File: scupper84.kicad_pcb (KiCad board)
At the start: 2 copper layers, 172 parts, among them K1 PG1350, K10 PG1350, K11 PG1350, K12 PG1350, K13 PG1350, K14 PG1350, K15 PG1350, K16 PG1350, K17 PG1350, K18 PG1350, K19 PG1350, K2 PG1350, K20 PG1350, K21 PG1350, K22 PG1350, K23 PG1350, K24 PG1350, K25 PG1350, K26 PG1350, K27 PG1350, K28 PG1350, K29 PG1350, K3 PG1350, K30 PG1350, K31 PG1350, K32 PG1350, K33 PG1350, K34 PG1350, K35 PG1350, K36 PG1350, K37 PG1350, K38 PG1350, K39 PG1350, K4 PG1350, K40 PG1350, K41 PG1350, K42 PG1350, K43 PG1350, K44 PG1350, K45 PG1350, K46 PG1350, K47 PG1350, K48 PG1350, K49 PG1350, K5 PG1350, K50 PG1350, K51 PG1350, K52 PG1350, K53 PG1350, K54 PG1350, K55 PG1350, K56 PG1350, K57 PG1350, K58 PG1350, K59 PG1350, K6 PG1350, K60 PG1350, K61 PG1350, K62 PG1350, K63 PG1350, K64 PG1350, K65 PG1350, K66 PG1350, K67 PG1350, K68 PG1350, K69 PG1350, K7 PG1350, K70 PG1350, K71 PG1350, K72 PG1350, K73 PG1350, K74 PG1350, K75 PG1350, K76 PG1350, K77 PG1350, K78 PG1350, K79 PG1350, K8 PG1350, K80 PG1350, K81 PG1350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

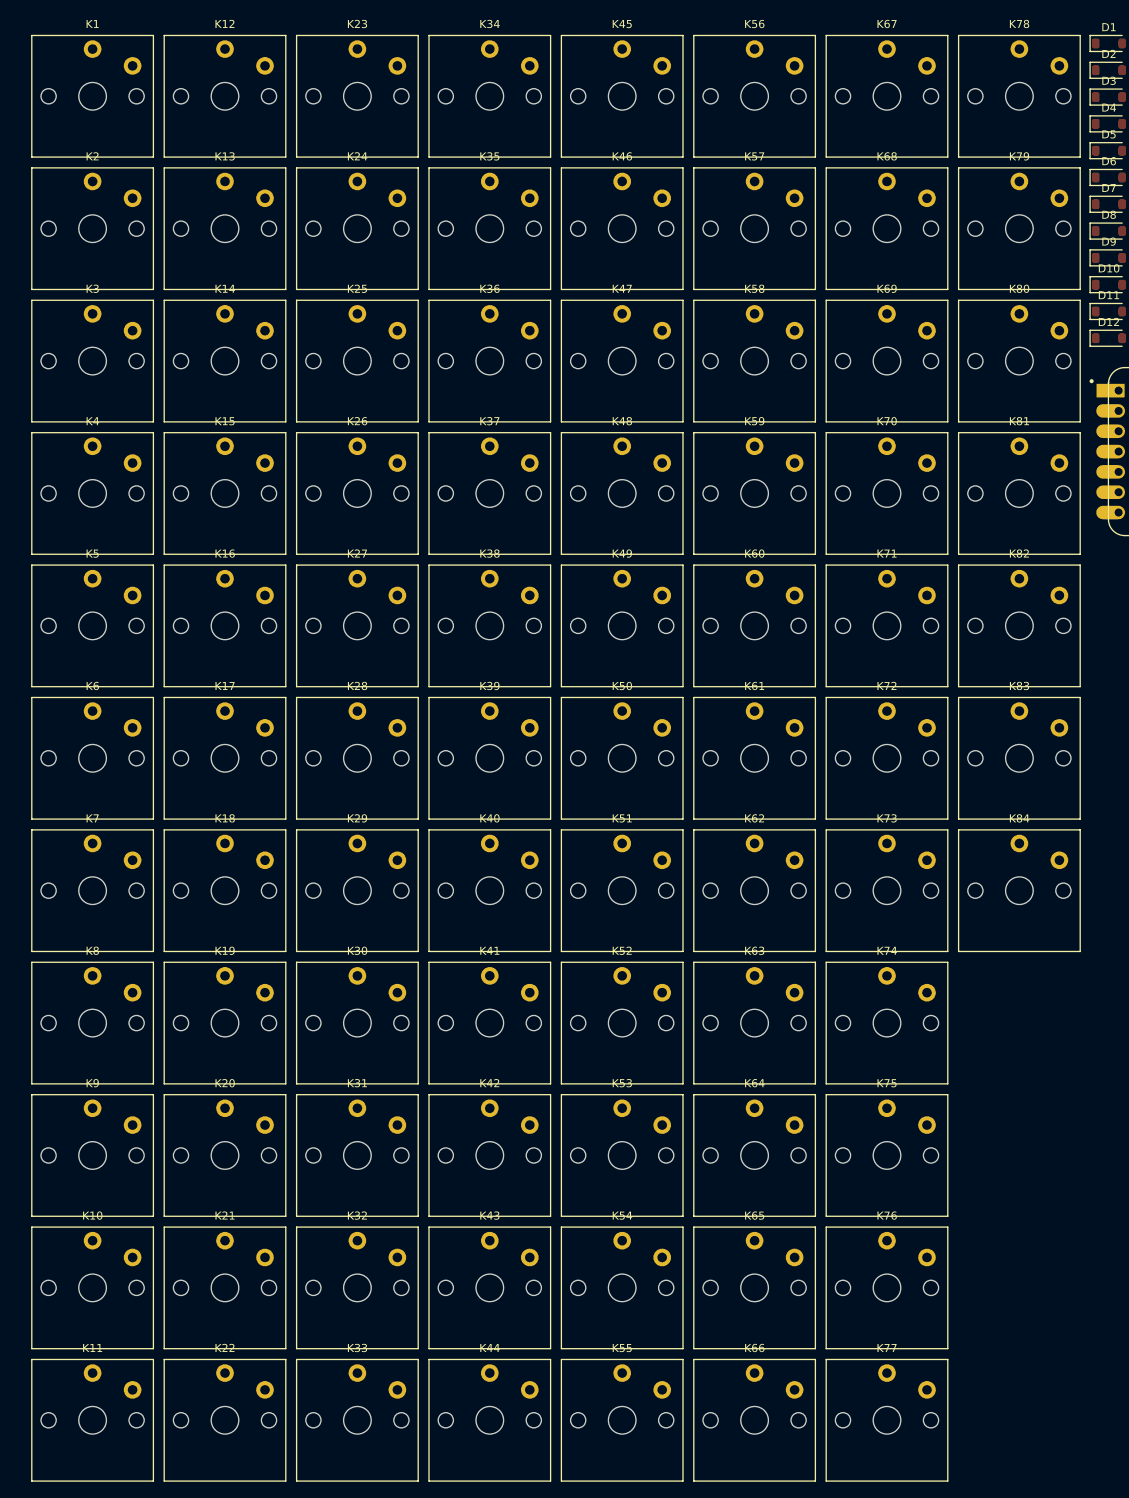
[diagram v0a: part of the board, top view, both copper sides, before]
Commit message: Work in progress on Kailh footprints.
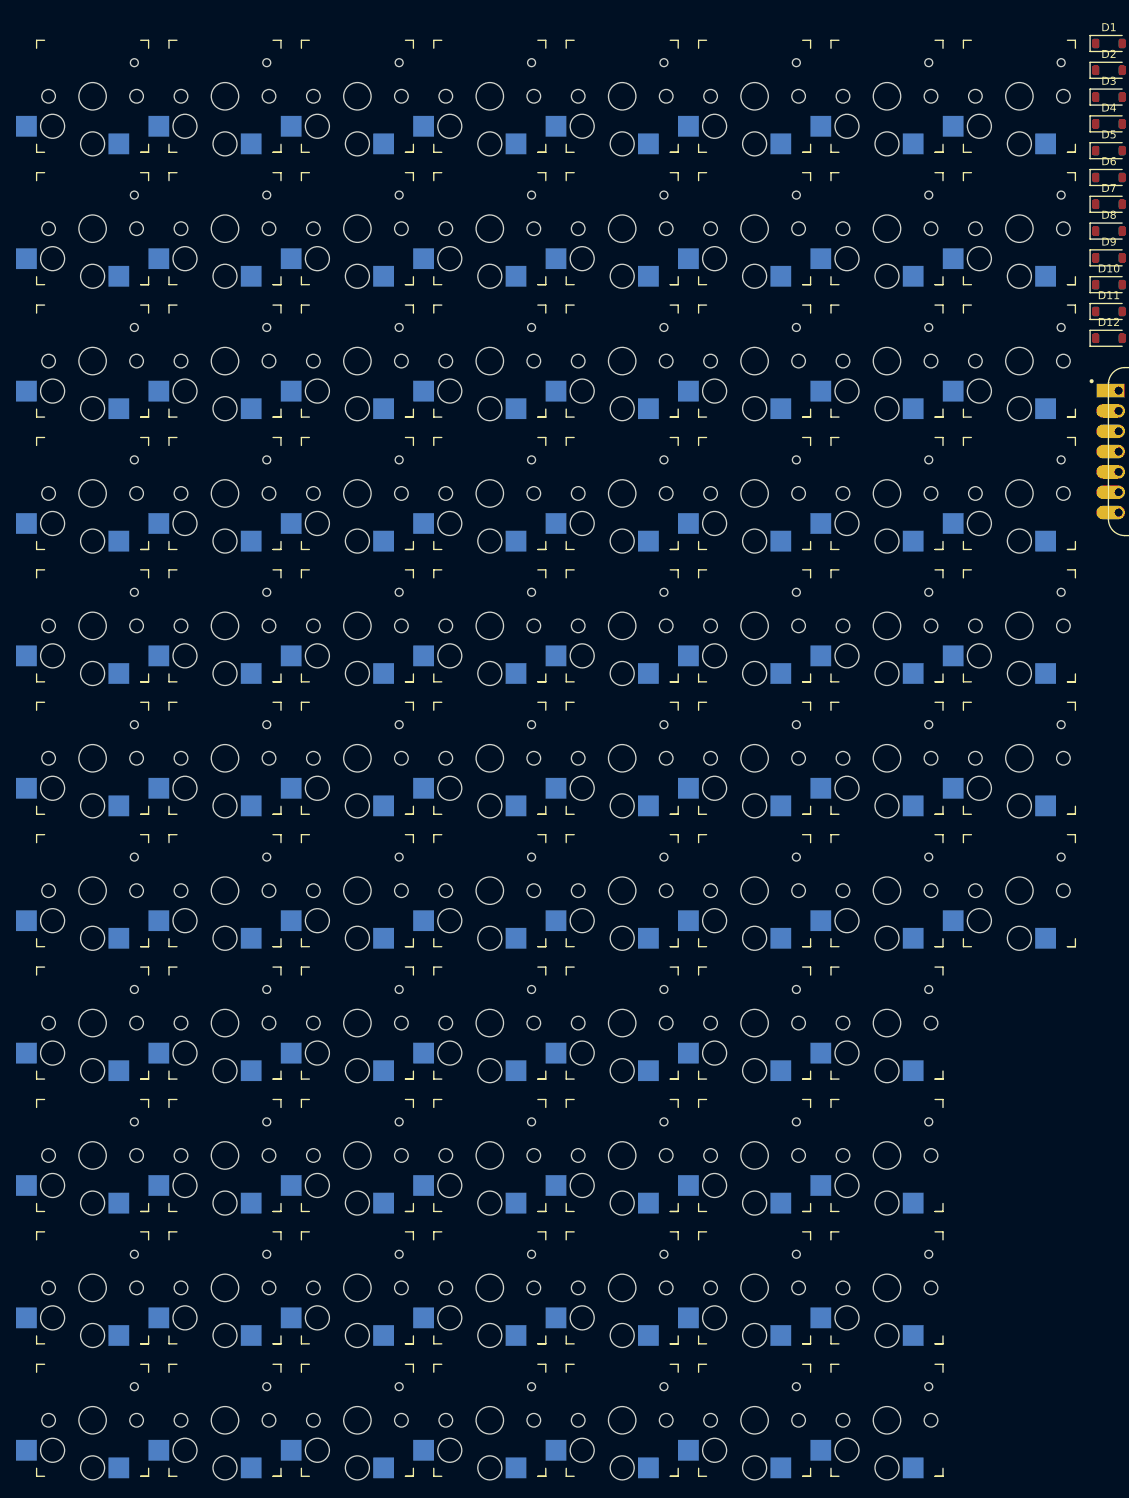
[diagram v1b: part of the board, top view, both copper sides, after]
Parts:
- K1, K10, K11, K12, K13, K14, K15, K16, K17, K18, K19, K2, K20, K21, K22, K23, K24, K25, K26, K27, K28, K29, K3, K30, K31, K32, K33, K34, K35, K36, K37, K38, K39, K4, K40, K41, K42, K43, K44, K45, K46, K47, K48, K49, K5, K50, K51, K52, K53, K54, K55, K56, K57, K58, K59, K6, K60, K61, K62, K63, K64, K65, K66, K67, K68, K69, K7, K70, K71, K72, K73, K74, K75, K76, K77, K78, K79, K8, K80, K81, K82, K83, K84, K9: footprint Switch_Keyboard_Kailh:SW_Kailh_Choc_V1 -> keyswitches:Kailh_socket_PG1350

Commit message: Arranging keys in their staggered array. Keys bigger than 1u may still need some adjustment.
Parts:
- added C1: C, Capacitor_SMD:C_1206_3216Metric_Pad1.33x1.80mm_HandSolder, F.Cu at (134.4, 196.0)
- added D85: 1N4001, Diode_THT:D_DO-41_SOD81_P10.16mm_Horizontal, F.Cu at (119.3, 196.4)
- added DS1: SK6812-E, keyboard_parts:LED_RGB_SK6812Mini-E, F.Cu at (121.6, 143.6)
- added DS10: SK6812-E, keyboard_parts:LED_RGB_SK6812Mini-E, F.Cu at (121.6, 183.2)
- added DS11: SK6812-E, keyboard_parts:LED_RGB_SK6812Mini-E, F.Cu at (121.6, 187.6)
- added DS12: SK6812-E, keyboard_parts:LED_RGB_SK6812Mini-E, F.Cu at (121.6, 192.0)
- added DS13: SK6812-E, keyboard_parts:LED_RGB_SK6812Mini-E, F.Cu at (129.9, 143.6)
- added DS14: SK6812-E, keyboard_parts:LED_RGB_SK6812Mini-E, F.Cu at (129.9, 148.0)
- added DS15: SK6812-E, keyboard_parts:LED_RGB_SK6812Mini-E, F.Cu at (129.9, 152.4)
- added DS16: SK6812-E, keyboard_parts:LED_RGB_SK6812Mini-E, F.Cu at (129.9, 156.8)
- added DS17: SK6812-E, keyboard_parts:LED_RGB_SK6812Mini-E, F.Cu at (129.9, 161.2)
- added DS18: SK6812-E, keyboard_parts:LED_RGB_SK6812Mini-E, F.Cu at (129.9, 165.6)
- added DS19: SK6812-E, keyboard_parts:LED_RGB_SK6812Mini-E, F.Cu at (129.9, 170.0)
- added DS2: SK6812-E, keyboard_parts:LED_RGB_SK6812Mini-E, F.Cu at (121.6, 148.0)
- added DS20: SK6812-E, keyboard_parts:LED_RGB_SK6812Mini-E, F.Cu at (129.9, 174.4)
- added DS21: SK6812-E, keyboard_parts:LED_RGB_SK6812Mini-E, F.Cu at (129.9, 178.8)
- added DS22: SK6812-E, keyboard_parts:LED_RGB_SK6812Mini-E, F.Cu at (129.9, 183.2)
- added DS23: SK6812-E, keyboard_parts:LED_RGB_SK6812Mini-E, F.Cu at (129.9, 187.6)
- added DS24: SK6812-E, keyboard_parts:LED_RGB_SK6812Mini-E, F.Cu at (129.9, 192.0)
- added DS25: SK6812-E, keyboard_parts:LED_RGB_SK6812Mini-E, F.Cu at (138.1, 143.6)
- added DS26: SK6812-E, keyboard_parts:LED_RGB_SK6812Mini-E, F.Cu at (138.1, 148.0)
- added DS27: SK6812-E, keyboard_parts:LED_RGB_SK6812Mini-E, F.Cu at (138.1, 152.4)
- added DS28: SK6812-E, keyboard_parts:LED_RGB_SK6812Mini-E, F.Cu at (138.1, 156.8)
- added DS29: SK6812-E, keyboard_parts:LED_RGB_SK6812Mini-E, F.Cu at (138.1, 161.2)
- added DS3: SK6812-E, keyboard_parts:LED_RGB_SK6812Mini-E, F.Cu at (121.6, 152.4)
- added DS30: SK6812-E, keyboard_parts:LED_RGB_SK6812Mini-E, F.Cu at (138.1, 165.6)
- added DS31: SK6812-E, keyboard_parts:LED_RGB_SK6812Mini-E, F.Cu at (138.1, 170.0)
- added DS32: SK6812-E, keyboard_parts:LED_RGB_SK6812Mini-E, F.Cu at (138.1, 174.4)
- added DS33: SK6812-E, keyboard_parts:LED_RGB_SK6812Mini-E, F.Cu at (138.1, 178.8)
- added DS34: SK6812-E, keyboard_parts:LED_RGB_SK6812Mini-E, F.Cu at (138.1, 183.2)
- added DS35: SK6812-E, keyboard_parts:LED_RGB_SK6812Mini-E, F.Cu at (138.1, 187.6)
- added DS36: SK6812-E, keyboard_parts:LED_RGB_SK6812Mini-E, F.Cu at (138.1, 192.0)
- added DS37: SK6812-E, keyboard_parts:LED_RGB_SK6812Mini-E, F.Cu at (146.4, 143.6)
- added DS38: SK6812-E, keyboard_parts:LED_RGB_SK6812Mini-E, F.Cu at (146.4, 148.0)
- added DS39: SK6812-E, keyboard_parts:LED_RGB_SK6812Mini-E, F.Cu at (146.4, 152.4)
- added DS4: SK6812-E, keyboard_parts:LED_RGB_SK6812Mini-E, F.Cu at (121.6, 156.8)
- added DS40: SK6812-E, keyboard_parts:LED_RGB_SK6812Mini-E, F.Cu at (146.4, 156.8)
- added DS41: SK6812-E, keyboard_parts:LED_RGB_SK6812Mini-E, F.Cu at (146.4, 161.2)
- added DS42: SK6812-E, keyboard_parts:LED_RGB_SK6812Mini-E, F.Cu at (146.4, 165.6)
- added DS43: SK6812-E, keyboard_parts:LED_RGB_SK6812Mini-E, F.Cu at (146.4, 170.0)
- added DS44: SK6812-E, keyboard_parts:LED_RGB_SK6812Mini-E, F.Cu at (146.4, 174.4)
- added DS45: SK6812-E, keyboard_parts:LED_RGB_SK6812Mini-E, F.Cu at (146.4, 178.8)
- added DS46: SK6812-E, keyboard_parts:LED_RGB_SK6812Mini-E, F.Cu at (146.4, 183.2)
- added DS47: SK6812-E, keyboard_parts:LED_RGB_SK6812Mini-E, F.Cu at (146.4, 187.6)
- added DS48: SK6812-E, keyboard_parts:LED_RGB_SK6812Mini-E, F.Cu at (146.4, 192.0)
- added DS49: SK6812-E, keyboard_parts:LED_RGB_SK6812Mini-E, F.Cu at (154.7, 143.6)
- added DS5: SK6812-E, keyboard_parts:LED_RGB_SK6812Mini-E, F.Cu at (121.6, 161.2)
- added DS50: SK6812-E, keyboard_parts:LED_RGB_SK6812Mini-E, F.Cu at (154.7, 148.0)
- added DS51: SK6812-E, keyboard_parts:LED_RGB_SK6812Mini-E, F.Cu at (154.7, 152.4)
- added DS52: SK6812-E, keyboard_parts:LED_RGB_SK6812Mini-E, F.Cu at (154.7, 156.8)
- added DS53: SK6812-E, keyboard_parts:LED_RGB_SK6812Mini-E, F.Cu at (154.7, 161.2)
- added DS54: SK6812-E, keyboard_parts:LED_RGB_SK6812Mini-E, F.Cu at (154.7, 165.6)
- added DS55: SK6812-E, keyboard_parts:LED_RGB_SK6812Mini-E, F.Cu at (154.7, 170.0)
- added DS56: SK6812-E, keyboard_parts:LED_RGB_SK6812Mini-E, F.Cu at (154.7, 174.4)
- added DS57: SK6812-E, keyboard_parts:LED_RGB_SK6812Mini-E, F.Cu at (154.7, 178.8)
- added DS58: SK6812-E, keyboard_parts:LED_RGB_SK6812Mini-E, F.Cu at (154.7, 183.2)
- added DS59: SK6812-E, keyboard_parts:LED_RGB_SK6812Mini-E, F.Cu at (154.7, 187.6)
- added DS6: SK6812-E, keyboard_parts:LED_RGB_SK6812Mini-E, F.Cu at (121.6, 165.6)
- added DS60: SK6812-E, keyboard_parts:LED_RGB_SK6812Mini-E, F.Cu at (154.7, 192.0)
- added DS61: SK6812-E, keyboard_parts:LED_RGB_SK6812Mini-E, F.Cu at (163.0, 143.6)
- added DS62: SK6812-E, keyboard_parts:LED_RGB_SK6812Mini-E, F.Cu at (163.0, 148.0)
- added DS63: SK6812-E, keyboard_parts:LED_RGB_SK6812Mini-E, F.Cu at (163.0, 152.4)
- added DS64: SK6812-E, keyboard_parts:LED_RGB_SK6812Mini-E, F.Cu at (163.0, 156.8)
- added DS65: SK6812-E, keyboard_parts:LED_RGB_SK6812Mini-E, F.Cu at (163.0, 161.2)
- added DS66: SK6812-E, keyboard_parts:LED_RGB_SK6812Mini-E, F.Cu at (163.0, 165.6)
- added DS67: SK6812-E, keyboard_parts:LED_RGB_SK6812Mini-E, F.Cu at (163.0, 170.0)
- added DS68: SK6812-E, keyboard_parts:LED_RGB_SK6812Mini-E, F.Cu at (163.0, 174.4)
- added DS69: SK6812-E, keyboard_parts:LED_RGB_SK6812Mini-E, F.Cu at (163.0, 178.8)
- added DS7: SK6812-E, keyboard_parts:LED_RGB_SK6812Mini-E, F.Cu at (121.6, 170.0)
- added DS70: SK6812-E, keyboard_parts:LED_RGB_SK6812Mini-E, F.Cu at (163.0, 183.2)
- added DS71: SK6812-E, keyboard_parts:LED_RGB_SK6812Mini-E, F.Cu at (163.0, 187.6)
- added DS72: SK6812-E, keyboard_parts:LED_RGB_SK6812Mini-E, F.Cu at (163.0, 192.0)
- added DS73: SK6812-E, keyboard_parts:LED_RGB_SK6812Mini-E, F.Cu at (171.2, 143.6)
- added DS74: SK6812-E, keyboard_parts:LED_RGB_SK6812Mini-E, F.Cu at (171.2, 148.0)
- added DS75: SK6812-E, keyboard_parts:LED_RGB_SK6812Mini-E, F.Cu at (171.2, 152.4)
- added DS76: SK6812-E, keyboard_parts:LED_RGB_SK6812Mini-E, F.Cu at (171.2, 156.8)
- added DS77: SK6812-E, keyboard_parts:LED_RGB_SK6812Mini-E, F.Cu at (171.2, 161.2)
- added DS78: SK6812-E, keyboard_parts:LED_RGB_SK6812Mini-E, F.Cu at (171.2, 165.6)
- added DS79: SK6812-E, keyboard_parts:LED_RGB_SK6812Mini-E, F.Cu at (171.2, 170.0)
- added DS8: SK6812-E, keyboard_parts:LED_RGB_SK6812Mini-E, F.Cu at (121.6, 174.4)
- added DS80: SK6812-E, keyboard_parts:LED_RGB_SK6812Mini-E, F.Cu at (171.2, 174.4)
- added DS81: SK6812-E, keyboard_parts:LED_RGB_SK6812Mini-E, F.Cu at (171.2, 178.8)
- added DS82: SK6812-E, keyboard_parts:LED_RGB_SK6812Mini-E, F.Cu at (171.2, 183.2)
- added DS83: SK6812-E, keyboard_parts:LED_RGB_SK6812Mini-E, F.Cu at (171.2, 187.6)
- added DS84: SK6812-E, keyboard_parts:LED_RGB_SK6812Mini-E, F.Cu at (171.2, 192.0)
- added DS9: SK6812-E, keyboard_parts:LED_RGB_SK6812Mini-E, F.Cu at (121.6, 178.8)
- K1, K10, K11, K12, K13, K14, K15, K16, K17, K18, K19, K2, K20, K21, K22, K23, K24, K25, K26, K27, K28, K29, K3, K30, K31, K32, K33, K34, K35, K36, K37, K38, K39, K4, K40, K41, K42, K43, K44, K45, K46, K47, K48, K49, K5, K50, K51, K52, K53, K54, K55, K56, K57, K58, K59, K6, K60, K61, K62, K63, K64, K65, K66, K67, K68, K69, K7, K70, K71, K72, K73, K74, K75, K76, K77, K78, K79, K8, K80, K81, K82, K83, K84, K9: footprint keyswitches:Kailh_socket_PG1350 -> keyboard_parts:Socket_PG1350_Hotswap
- moved K15 238.5 mm to (276.2, 42.5)
- moved K30 233.7 mm to (276.2, 59.5)
- moved K11 222.1 mm to (191.2, 42.5)
- moved K14 220.1 mm to (259.2, 42.5)
- moved K44 213.5 mm to (255.0, 76.5)
- moved K29 204.2 mm to (250.8, 59.5)
- moved K10 198.4 mm to (174.2, 42.5)
- moved K45 194.8 mm to (276.2, 76.5)
- moved K43 186.7 mm to (233.8, 76.5)
- moved K13 185.7 mm to (225.2, 42.5)
- moved K28 175.1 mm to (225.2, 59.5)
- moved K9 174.8 mm to (157.2, 42.5)
- moved K59 171.9 mm to (276.2, 93.5)
- moved K12 169.9 mm to (208.2, 42.5)
- moved K42 163.8 mm to (216.8, 76.5)
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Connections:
- U1 pad 14: unconnected-(U1-5V-Pad14) -> +5V
- U1 pad 7: unconnected-(U1-D6-Pad7) -> glow0
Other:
- board outline added: 3.2 x 2.8 mm

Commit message: Repositioning RGB LEDs with a script.
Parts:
- moved DS15 185.9 mm to (276.2, 37.8)
- moved DS30 177.1 mm to (276.2, 54.8)
- moved DS12 176.9 mm to (208.2, 37.8)
- moved DS14 170.0 mm to (259.2, 37.8)
- moved DS45 168.3 mm to (276.2, 71.8)
- moved DS11 165.2 mm to (191.2, 37.8)
- moved DS59 156.7 mm to (276.2, 88.8)
- moved DS29 155.0 mm to (250.8, 54.8)
- moved DS10 154.7 mm to (174.2, 37.8)
- moved DS46 151.7 mm to (27.6, 88.8)
- moved DS60 150.1 mm to (31.9, 105.8)
- moved DS74 150.0 mm to (23.4, 122.8)
- moved DS31 149.4 mm to (25.5, 71.8)
- moved DS44 149.4 mm to (255.0, 71.8)
- moved DS16 149.0 mm to (21.2, 54.8)
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
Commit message: Provisionally placing shift registers and stuff. I should position them precisely before planning any builds.
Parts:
- moved C1 196.1 mm to (30.1, 29.9), turned to 180 degrees
- moved D85 195.1 mm to (20.2, 28.4), turned to 90 degrees
- moved U3 185.1 mm to (195.4, 22.3), turned to -90 degrees
- moved SW1 182.9 mm to (133.6, 15.3), turned to 90 degrees
- moved U2 165.2 mm to (86.0, 23.4), turned to 90 degrees
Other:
- board size 3.2 x 2.8 mm -> 276.9 x 127.3 mm

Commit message: Messing around with keycap placement.
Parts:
- moved D37 60.5 mm to (155.6, 158.6)
- moved D38 60.5 mm to (155.6, 161.9)
- moved D39 60.5 mm to (155.6, 165.2)
- moved D40 60.5 mm to (155.6, 168.6)
- moved D42 60.5 mm to (155.6, 175.3)
- moved D43 60.5 mm to (155.6, 178.7)
- moved D44 60.5 mm to (155.6, 182.0)
- moved D45 60.5 mm to (155.6, 185.3)
- moved D47 60.5 mm to (155.6, 192.1)
- moved D48 60.5 mm to (155.6, 195.4)
- moved D61 60.5 mm to (167.2, 158.6)
- moved D62 60.5 mm to (167.2, 161.9)
- moved D63 60.5 mm to (167.2, 165.2)
- moved D64 60.5 mm to (167.2, 168.6)
- moved D66 60.5 mm to (167.2, 175.3)
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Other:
- board text added: "1.25U"
- board text added: "1.5U"
- board text added: "1.75U"
- board text added: "16.5mm x 16.5mm"
- board text added: "1U"
- board text added: "2.25U"
- board text added: "2.5U"
- board text added: "21.25mm x 16.5mm"
- board text added: "26mm x 16.5mm"
- board text added: "30.5mm x 16.5mm"
- board text added: "35.5mm x 16.5mm"
- board text added: "3U"
- board text added: "40.5mm x 16.5mm"
- board text added: "54.5mm x 16.5mm"

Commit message: Centering switches under keycaps that moved.
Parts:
- moved K77 3.20 mm to (97.0, 127.5)
- moved K78 3.20 mm to (152.1, 127.5)
- moved K79 3.20 mm to (188.1, 127.5)
- moved K80 3.20 mm to (205.1, 127.5)
- moved K81 3.20 mm to (222.1, 127.5)
- moved K72 2.79 mm to (256.5, 111.0)
- moved K82 2.79 mm to (239.5, 128.0)
- moved K83 2.79 mm to (256.5, 128.0)
- moved K84 2.79 mm to (273.5, 128.0)
- moved K14 2.30 mm to (256.9, 42.5)
- moved K15 2.30 mm to (273.9, 42.5)
- moved K30 2.30 mm to (273.9, 59.5)
- moved K45 2.30 mm to (273.9, 76.5)
- moved K59 2.30 mm to (273.9, 93.5)
- moved K73 2.30 mm to (273.9, 110.5)
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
